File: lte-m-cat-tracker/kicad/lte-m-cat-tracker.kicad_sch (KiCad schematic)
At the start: 32 parts, among them J1 JST-GH-1.25mm-2P, J2 USB-C-16P, SW1 MSK12C02, U1 SIM7080G-M, U2 ESP32-C3, U3 LIS2DW12TR, U4 TP4056, U5 XC6220B331MR-G

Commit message: schematic: STEP2回路修正4件完了（2026-06-07）
- J1: JST-GH 1.25mm (C160404) → JST-PH 2mm 2P (C295747, 定格2A)
- C13追加: VBAT直近 100μF 6.3V polymer 1210（LCSCは発注前要確認）
- U3 SDO/SA0 (pin1): no_connect → GND接続（I2Cアドレス0x18固定）
- ANT3 LCSC: 空 → C7464606（2450AT18A100・発注前要確認）

Co-Authored-By: Claude Sonnet 4.6 <noreply@anthropic.com>
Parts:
- added C13: 100uF_6.3V_PolymerAl, Capacitor_SMD:C_1210_3225Metric, symbol Device:C
- ANT3: LCSC (none) -> C7464606
- J1: value JST-GH-1.25mm-2P -> JST-PH-2mm-2P; footprint Connector_JST:JST_GH_SM02B-GHS-TB_1x02-1MP_P1.25mm_Horizontal -> Connector_JST:JST_PH_S2B-PH-K-S_1x02_P2.00mm_Horizontal; LCSC C160404 -> C295747
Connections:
- net GND: now also U3.5 (INT2), C13.2
- net VBAT: now also C13.1
- no-connect marks 28 -> 27
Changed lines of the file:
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@@
     (exclude_from_sim no)(in_bom yes)(on_board yes)
     (property "Reference" "J1" (at 114.3 67.62 0)(effects(font(size 1.27 1.27))))
-    (property "Value" "JST-GH-1.25mm-2P" (at 114.3 69.12 0)(effects(font(size 1.27 1.27))))
-    (property "Footprint" "Connector_JST:JST_GH_SM02B-GHS-TB_1x02-1MP_P1.25mm_Horizontal" (at 114.3 71.12 0)(effects(font(size 1.27 1.27))hide))
-    (property "LCSC" "C160404" (at 114.3 71.12 0)(effects(font(size 1.27 1.27))hide))
+    (property "Value" "JST-PH-2mm-2P" (at 114.3 69.12 0)(effects(font(size 1.27 1.27))))
+    (property "Footprint" "Connector_JST:JST_PH_S2B-PH-K-S_1x02_P2.00mm_Horizontal" (at 114.3 71.12 0)(effects(font(size 1.27 1.27))hide))
+    (property "LCSC" "C295747" (at 114.3 71.12 0)(effects(font(size 1.27 1.27))hide))
   )
   (label "VBAT" (at 104.14 69.85 180)
@@
     (property "Value" "GND"(at 104.14 73.66 0)(effects(font(size 1.27 1.27))))
     (property "Footprint" ""(at 104.14 72.39 0)(effects(font(size 1.27 1.27))hide)))
+  (symbol (lib_id "Device:C") (at 104.14 82.55 0) (unit 1)
+    (exclude_from_sim no)(in_bom yes)(on_board yes)
+    (property "Reference" "C13" (at 107.95 80.645 0)(effects(font(size 1.27 1.27))))
+    (property "Value" "100uF_6.3V_PolymerAl" (at 107.95 83.185 0)(effects(font(size 1.27 1.27))))
+    (property "Footprint" "Capacitor_SMD:C_1210_3225Metric" (at 104.14 82.55 0)(effects(font(size 1.27 1.27))hide))
+    (property "LCSC" "要LCSC確認" (at 104.14 82.55 0)(effects(font(size 1.27 1.27))hide))
+  )
+  (label "VBAT" (at 104.14 78.74 270)
+    (effects(font(size 1.27 1.27))(justify left))
+)
+  (symbol (lib_id "power:GND") (at 104.14 86.36 0)(unit 1)
+    (exclude_from_sim no)(in_bom no)(on_board no)
+    (property "Reference" "#PWR"(at 104.14 88.9 0)(effects(font(size 1.27 1.27))hide))
+    (property "Value" "GND"(at 104.14 87.63 0)(effects(font(size 1.27 1.27))))
+    (property "Footprint" ""(at 104.14 86.36 0)(effects(font(size 1.27 1.27))hide)))
   (symbol (lib_id "Regulator_Linear:XC6220B331MR") (at 119.38 96.52 0) (unit 1)
     (exclude_from_sim no)(in_bom yes)(on_board yes)
@@
     (property "Value" "2450AT18A100" (at 45.72 198.66 0)(effects(font(size 1.27 1.27))))
     (property "Footprint" "lte-m-custom:ChipAntenna_2x1.25mm" (at 45.72 200.66 0)(effects(font(size 1.27 1.27))hide))
-    (property "LCSC" "" (at 45.72 200.66 0)(effects(font(size 1.27 1.27))hide))
+    (property "LCSC" "C7464606" (at 45.72 200.66 0)(effects(font(size 1.27 1.27))hide))
   )
   (label "WIFI_ANT" (at 40.64 200.66 180)
@@
     (property "Value" "GND"(at 228.6 196.85000000000002 0)(effects(font(size 1.27 1.27))))
     (property "Footprint" ""(at 228.6 195.58 0)(effects(font(size 1.27 1.27))hide)))
-  (no_connect (at 228.6 205.74))
+  (symbol (lib_id "power:GND") (at 228.6 205.74 0)(unit 1)
+    (exclude_from_sim no)(in_bom no)(on_board no)
+    (property "Reference" "#PWR"(at 228.6 208.28 0)(effects(font(size 1.27 1.27))hide))
+    (property "Value" "GND"(at 228.6 207.01 0)(effects(font(size 1.27 1.27))))
+    (property "Footprint" ""(at 228.6 205.74 0)(effects(font(size 1.27 1.27))hide)))
   (no_connect (at 259.08 195.58))
   (no_connect (at 259.08 198.12))

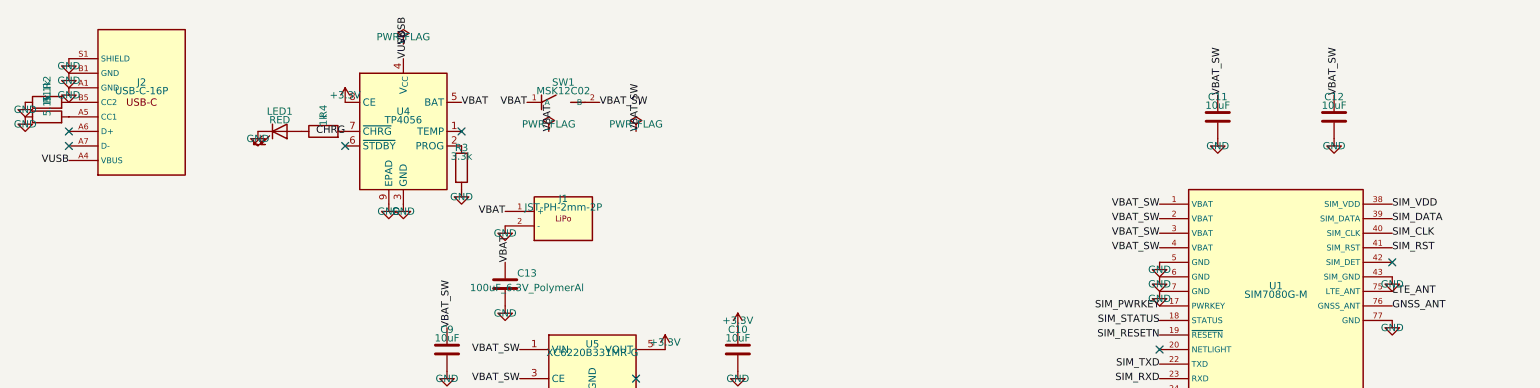
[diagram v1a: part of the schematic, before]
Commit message: SCH: BLOCK-1/2/5/6/8 回路図修正
- BLOCK-1: PROG ネット追加（U4.PROG ↔ R3.pin2）
- BLOCK-2: CC1直結GND削除・CC1/CC2ラベル追加（R1/R2経由5.1kΩプルダウン正規化）
- BLOCK-5: C14 100nF/0402 VBAT_SW デカップリング追加（U1向け）
- BLOCK-6: C15 100nF/0402 VBAT_SW デカップリング追加（U5向け）
- BLOCK-8: LED_ANODE ネット追加（R4.pin2 ↔ LED1.anode）

Co-Authored-By: Claude Sonnet 4.6 <noreply@anthropic.com>
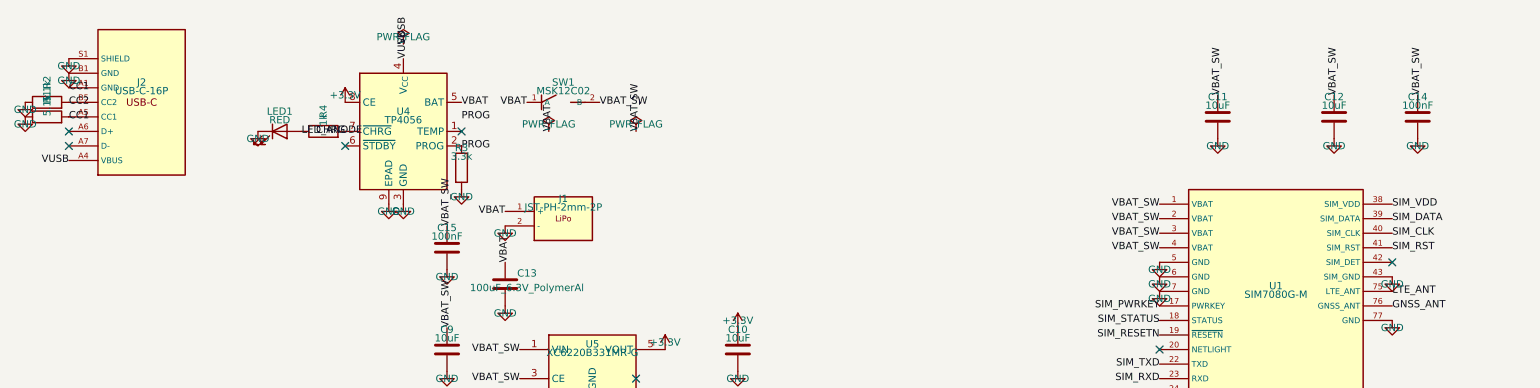
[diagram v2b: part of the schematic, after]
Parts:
- added C14, C15: 100nF, Capacitor_SMD:C_0402_1005Metric, symbol Device:C
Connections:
- net GND: now also C14.2, C15.2; no longer J2.A1 (GND)
- net VBAT_SW: now also C14.1, C15.1
- net CC2: now reaches J2.B5 (CC2), R2.2
- net CC1: now reaches J2.A5 (CC1), R1.2
- net CC1: now also J2.A1 (GND)
- net LED_ANODE: now reaches LED1.2 (A), R4.1
- net PROG: now reaches R3.1, U4.2 (PROG)
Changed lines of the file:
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@@
   (no_connect (at 27.94 58.42))
   (no_connect (at 27.94 55.88))
-  (symbol (lib_id "power:GND") (at 27.94 48.26 0)(unit 1)
-    (exclude_from_sim no)(in_bom no)(on_board no)
-    (property "Reference" "#PWR"(at 27.94 50.8 0)(effects(font(size 1.27 1.27))hide))
-    (property "Value" "GND"(at 27.94 49.53 0)(effects(font(size 1.27 1.27))))
-    (property "Footprint" ""(at 27.94 48.26 0)(effects(font(size 1.27 1.27))hide)))
   (symbol (lib_id "power:GND") (at 27.94 45.72 0)(unit 1)
     (exclude_from_sim no)(in_bom no)(on_board no)
@@
 )
   (sheet_instances(path "/"(page "1")))
-)
+  (label "PROG" (at 96.52 53.34 0)
+    (effects(font(size 1.27 1.27))(justify left))
+)
+  (label "PROG" (at 96.52 58.42 0)
+    (effects(font(size 1.27 1.27))(justify left))
+)
+  (label "CC1" (at 27.94 48.26 0)
+    (effects(font(size 1.27 1.27))(justify left))
+)
+  (label "CC1" (at 27.94 53.34 0)
+    (effects(font(size 1.27 1.27))(justify left))
+)
+  (label "CC2" (at 27.94 50.8 0)
+    (effects(font(size 1.27 1.27))(justify left))
+)
+  (label "LED_ANODE" (at 68.58 55.88 0)
+    (effects(font(size 1.27 1.27))(justify left))
+)
+  (symbol (lib_id "Device:C") (at 263.52 53.34 0) (unit 1)
+    (exclude_from_sim no)(in_bom yes)(on_board yes)
+    (property "Reference" "C14" (at 263.52 49.84 0)(effects(font(size 1.27 1.27))))
+    (property "Value" "100nF" (at 263.52 51.34 0)(effects(font(size 1.27 1.27))))
+    (property "Footprint" "Capacitor_SMD:C_0402_1005Metric" (at 263.52 53.34 0)(effects(font(size 1.27 1.27))hide))
+    (property "LCSC" "C14663" (at 263.52 53.34 0)(effects(font(size 1.27 1.27))hide))
+  )
+  (label "VBAT_SW" (at 263.52 49.53 270)
+    (effects(font(size 1.27 1.27))(justify left))
+)
+  (symbol (lib_id "power:GND") (at 263.52 57.15 0)(unit 1)
+    (exclude_from_sim no)(in_bom no)(on_board no)
+    (property "Reference" "#PWR"(at 263.52 59.69 0)(effects(font(size 1.27 1.27))hide))
+    (property "Value" "GND"(at 263.52 58.42 0)(effects(font(size 1.27 1.27))))
+    (property "Footprint" ""(at 263.52 57.15 0)(effects(font(size 1.27 1.27))hide)))
+  (symbol (lib_id "Device:C") (at 93.98 76.2 0) (unit 1)
+    (exclude_from_sim no)(in_bom yes)(on_board yes)
+    (property "Reference" "C15" (at 93.98 72.7 0)(effects(font(size 1.27 1.27))))
+    (property "Value" "100nF" (at 93.98 74.2 0)(effects(font(size 1.27 1.27))))
+    (property "Footprint" "Capacitor_SMD:C_0402_1005Metric" (at 93.98 76.2 0)(effects(font(size 1.27 1.27))hide))
+    (property "LCSC" "C14663" (at 93.98 76.2 0)(effects(font(size 1.27 1.27))hide))
+  )
+  (label "VBAT_SW" (at 93.98 72.39 270)
+    (effects(font(size 1.27 1.27))(justify left))
+)
+  (symbol (lib_id "power:GND") (at 93.98 80.01 0)(unit 1)
+    (exclude_from_sim no)(in_bom no)(on_board no)
+    (property "Reference" "#PWR"(at 93.98 82.55 0)(effects(font(size 1.27 1.27))hide))
+    (property "Value" "GND"(at 93.98 81.28 0)(effects(font(size 1.27 1.27))))
+    (property "Footprint" ""(at 93.98 80.01 0)(effects(font(size 1.27 1.27))hide)))
+)

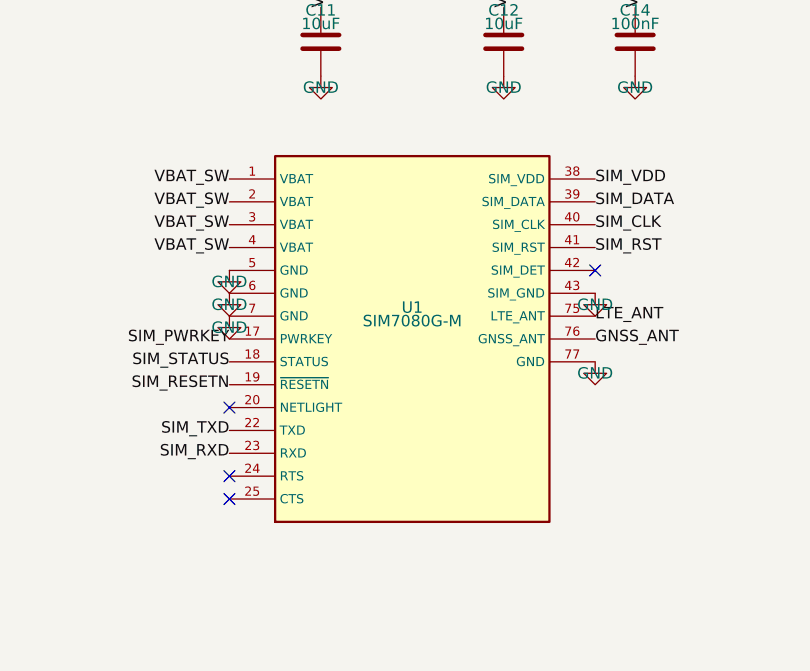
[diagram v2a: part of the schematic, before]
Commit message: フットプリント致命的バグ修正: SIM7080G-M 全77パッドを実座標に更新
- generate_footprints.py: LCC77フットプリントをHW Design V1.04+EasyEDA C18548266で修正
  - 全4辺ペリメーター、ピッチ1.10mm（旧: 推定1.80mm）
  - VBAT(pin34,35)を上辺に正しく配置（旧: 右辺に誤配置→電源不入）
  - RF_ANT(32)を右辺、GNSS_ANT(68)を内部LGA上辺右端に正しく配置
  - パッドサイズ: ピッチ方向0.90mm（0.20mmクリアランス確保）
- lte-m-cat-tracker.kicad_sch: シンボルピン番号を実モジュールに整合
  - RESETN→NC pad(28), SIM信号→下辺(15-19), LTE_ANT→32, GNSS_ANT→68
- lte-m-cat-tracker.kicad_pcb: U1フットプリントを新座標に置き換え
  - DRC: shorts=0件 ✅ / 未配線86件（配線再実行が次タスク）
- update_u1_footprint.py: PCB U1更新スクリプト追加
- DESIGN.md: 修正完了記録・新パッド座標表・次セッション手順を更新

Co-Authored-By: Claude Sonnet 4.6 <noreply@anthropic.com>
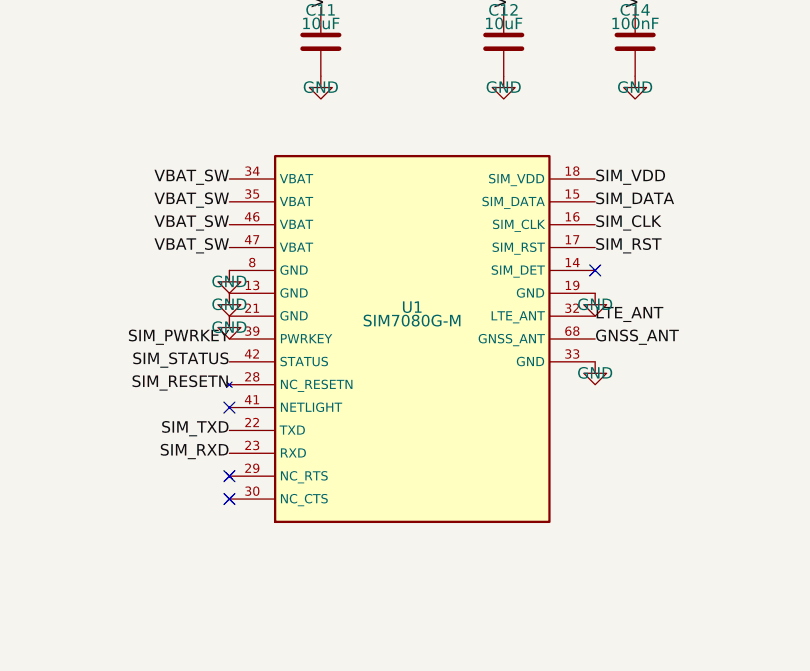
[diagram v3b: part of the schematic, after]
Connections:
- net GND: now also U1.13 (GND), U1.19 (GND), U1.21 (GND), U1.33 (GND), U1.8 (GND); no longer U1.43 (SIM_GND), U1.5 (GND), U1.6 (GND), U1.7 (GND), U1.77 (GND)
- net GNSS_ANT: now also U1.68 (GNSS_ANT); no longer U1.76 (GNSS_ANT)
- net LTE_ANT: now also U1.32 (LTE_ANT); no longer U1.75 (LTE_ANT)
- net SIM_CLK: now also U1.16 (SIM_CLK); no longer U1.40 (SIM_CLK)
- net SIM_DATA: now also U1.15 (SIM_DATA); no longer U1.39 (SIM_DATA)
- net SIM_PWRKEY: now also U1.39 (PWRKEY); no longer U1.17 (PWRKEY)
- net SIM_RESETN: now also U1.28 (NC_RESETN); no longer U1.19 (~{RESETN})
- net SIM_RST: now also U1.17 (SIM_RST); no longer U1.41 (SIM_RST)
- net SIM_STATUS: now also U1.42 (STATUS); no longer U1.18 (STATUS)
- net SIM_VDD: now also U1.18 (SIM_VDD); no longer U1.38 (SIM_VDD)
- net VBAT_SW: now also U1.34 (VBAT), U1.35 (VBAT), U1.46 (VBAT), U1.47 (VBAT); no longer U1.1 (VBAT), U1.2 (VBAT), U1.3 (VBAT), U1.4 (VBAT)

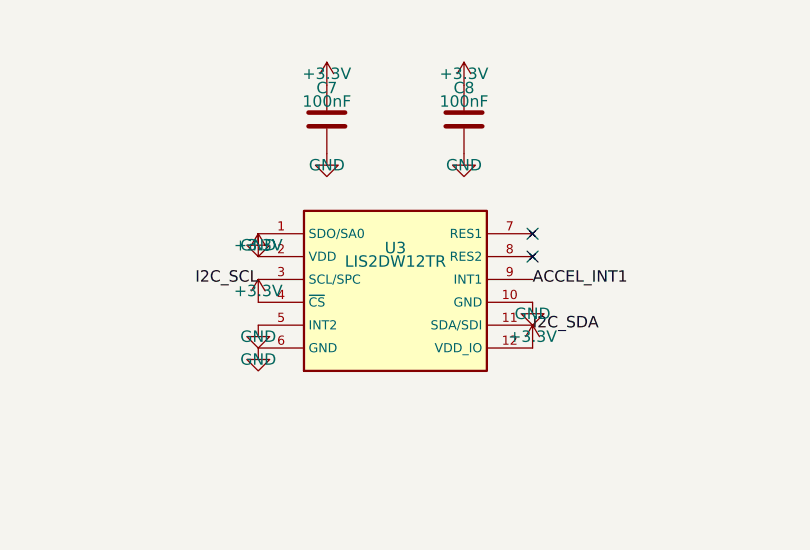
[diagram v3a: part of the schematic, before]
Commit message: CPL再生成(U3=180°)・回路図U3シンボル修正・BOM幽霊部品C14/C15削除・Gerber再出力
- CPLはPCBから直接生成（33部品・回転反映）
- 回路図U3ピン番号をST datasheet準拠に振り直し（配線変更ゼロで全ネット一致）
- ERC/DRC確認: 実shorts=0/crossings=0/unconnected=0維持
- 申し送り: U1 pin28のNC定義vs SIM_RESETN使用をレビューで要確認

Co-Authored-By: Claude Fable 5 <noreply@anthropic.com>
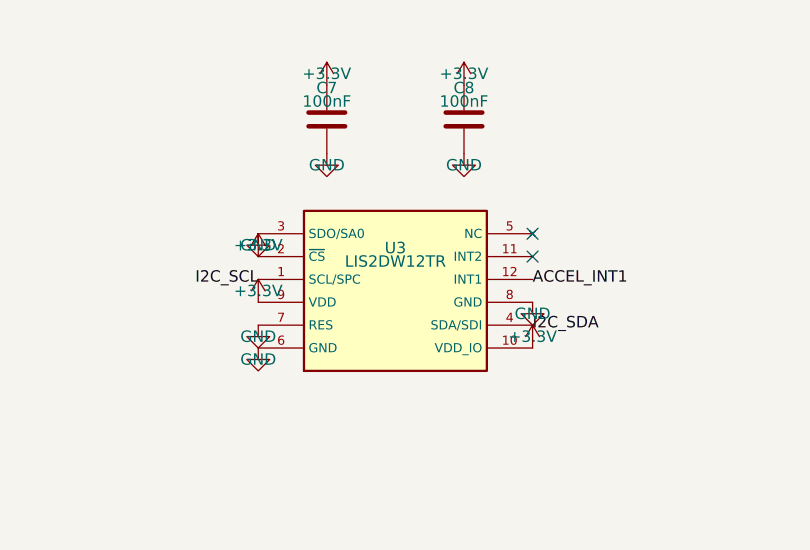
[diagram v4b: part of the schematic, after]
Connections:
- net +3.3V: now also U3.10 (VDD_IO), U3.9 (VDD); no longer U3.12 (VDD_IO), U3.4 (~{CS})
- net ACCEL_INT1: now also U3.12 (INT1); no longer U3.9 (INT1)
- net GND: now also U3.3 (SDO/SA0), U3.7 (RES), U3.8 (GND); no longer U3.1 (SDO/SA0), U3.10 (GND), U3.5 (INT2)
- net I2C_SCL: now also U3.1 (SCL/SPC); no longer U3.3 (SCL/SPC)
- net I2C_SDA: now also U3.4 (SDA/SDI); no longer U3.11 (SDA/SDI)
